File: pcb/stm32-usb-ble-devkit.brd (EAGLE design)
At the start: 90 x 50 mm, 98 parts, among them CN1 USB-MICROB-2TABS, CN2 USB-C-2.0-FEMALE, CN3 USB-C-2.0-FEMALE, Q2 AO3402, Q4 AO3401, Q6 AO3401, Q8 AO3401, U1 STM32F103-48LQFP, U2 STM32F205-64, U3 TUSB320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

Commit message: pcb: Replaced PSU BAS16 with better diode
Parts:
- D1: value BAS16 -> MBR0540T1; device tuetuopay:SOT23-3 -> tuetuopay:SOD123
- moved Q4 1.50 mm to (12.4, 47.4)
- moved D1 0.91 mm to (17.7, 47.2), turned to 0 degrees
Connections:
- net +5V: now also D1.C; no longer D1.3
- net STLINK_USB_VBUS: now also D1.A; no longer D1.1
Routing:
- net STLINK_USB_VBUS: track 41.4 -> 43.9 mm
- net +5V: track 65.0 -> 64.0 mm
- net USB_FS_HS_VBUS: track 6.31 -> 7.11 mm
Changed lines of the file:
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@@
 <attribute name="NAME" x="0.46" y="41.42" size="0.9" layer="25"/>
-</element>
-<element name="D1" library="tuetuopay" package="SOT23-3" value="BAS16" x="18.6" y="47.4" smashed="yes" rot="R270">
-<attribute name="NAME" x="20.03" y="49.21" size="0.9" layer="21" align="top-left"/>
 </element>
 <element name="JP10" library="pinhead" library_urn="urn:adsk.eagle:library:325" package="1X04" package3d_urn="urn:adsk.eagle:package:22407/2" value="" x="72.15" y="3.45" smashed="yes">
@@
 <attribute name="VALUE" x="39.637" y="14.07" size="1.27" layer="27" ratio="10" rot="R90"/>
 </element>
-<element name="Q4" library="tuetuopay" package="SOT23-3" value="AO3401" x="13.95" y="47.4" smashed="yes" rot="R270">
-<attribute name="NAME" x="15.23" y="46.36" size="0.9" layer="21" align="top-left"/>
+<element name="Q4" library="tuetuopay" package="SOT23-3" value="AO3401" x="12.45" y="47.4" smashed="yes" rot="R270">
+<attribute name="NAME" x="13.73" y="46.36" size="0.9" layer="21" align="top-left"/>
 </element>
 <element name="Q6" library="tuetuopay" package="SOT23-3" value="AO3401" x="15.45" y="12.3" smashed="yes" rot="R90">
@@
 <attribute name="NAME" x="61.615" y="22.765" size="0.9" layer="25" rot="R90"/>
 <attribute name="VALUE" x="59.295" y="21.635" size="1.27" layer="27" rot="R270"/>
+</element>
+<element name="D1" library="tuetuopay" package="SOD123" value="MBR0540T1" x="17.7" y="47.25" smashed="yes">
+<attribute name="NAME" x="16.75" y="48.4" size="0.9" layer="25"/>
+<attribute name="VALUE" x="16.6" y="44.95" size="1.27" layer="27"/>
 </element>
 </elements>
@@
 <via x="10.2" y="48.6" extent="1-16" drill="0.3"/>
 <via x="16.2" y="49.2" extent="1-16" drill="0.3"/>
-<via x="18" y="45" extent="1-16" drill="0.3"/>
+<via x="17.85" y="41.7" extent="1-16" drill="0.3"/>
 <via x="25.65" y="44.55" extent="1-16" drill="0.3"/>
 <via x="28.2" y="39.6" extent="1-16" drill="0.3"/>
@@
 <via x="71.4" y="7.8" extent="1-16" drill="0.3"/>
 <via x="54.6" y="9.6" extent="1-16" drill="0.3"/>
-<via x="12.6" y="40.35" extent="1-16" drill="0.3"/>
+<via x="12.75" y="42" extent="1-16" drill="0.3"/>
 <via x="13.5" y="39.6" extent="1-16" drill="0.3"/>
 <via x="4.35" y="27.3" extent="1-16" drill="0.3"/>
@@
 <via x="41.1" y="2.7" extent="1-16" drill="0.3"/>
 <via x="28.2" y="14.55" extent="1-16" drill="0.3"/>
-<via x="21.15" y="48" extent="1-16" drill="0.3"/>
+<via x="21.15" y="46.05" extent="1-16" drill="0.3"/>
 <via x="32.4" y="46.05" extent="1-16" drill="0.3"/>
 <via x="40.05" y="45.9" extent="1-16" drill="0.3"/>
@@
 <contactref element="U1" pad="47"/>
 <contactref element="R1" pad="2"/>
+<via x="16.2" y="45.9" extent="1-16" drill="0.3"/>
 </signal>
 <signal name="STLINK_PC13">
@@
 <contactref element="R16" pad="2"/>
 <contactref element="Q4" pad="1"/>
-<contactref element="D1" pad="1"/>
 <wire x1="44.03" y1="45.885" x2="44.03" y2="46.72" width="0.4" layer="1"/>
 <wire x1="44.03" y1="46.72" x2="43.65" y2="47.1" width="0.4" layer="1"/>
 <wire x1="44.03" y1="46.72" x2="50.67" y2="46.72" width="0.15" layer="1"/>
 <wire x1="50.67" y1="46.72" x2="51.7875" y2="47.85" width="0.15" layer="1"/>
-<wire x1="34.693" y1="47.1" x2="32.795" y2="48.998" width="0.4" layer="1"/>
-<wire x1="18.448" y1="48.998" x2="17.875" y2="48.425" width="0.4" layer="1"/>
+<wire x1="32.795" y1="48.998" x2="34.693" y2="47.1" width="0.4" layer="1"/>
 <wire x1="43.65" y1="47.1" x2="34.693" y2="47.1" width="0.4" layer="1"/>
-<wire x1="32.795" y1="48.998" x2="18.448" y2="48.998" width="0.4" layer="1"/>
-<wire x1="12.85" y1="48.35" x2="14.1" y2="48.35" width="0.4" layer="1"/>
-<wire x1="14.1" y1="48.35" x2="17.5" y2="48.35" width="0.4" layer="1"/>
-<wire x1="17.5" y1="48.35" x2="17.875" y2="48.425" width="0.4" layer="1"/>
+<contactref element="D1" pad="A"/>
+<wire x1="11.35" y1="48.35" x2="18.5" y2="48.35" width="0.4" layer="1"/>
+<wire x1="18.5" y1="48.35" x2="19.6" y2="47.25" width="0.4" layer="1"/>
+<wire x1="19.6" y1="47.25" x2="21.348" y2="48.998" width="0.4" layer="1"/>
+<wire x1="21.348" y1="48.998" x2="32.795" y2="48.998" width="0.4" layer="1"/>
 </signal>
 <signal name="STM_OSC_IN">
@@
 <contactref element="Q6" pad="2"/>
 <contactref element="Q8" pad="2"/>
-<contactref element="D1" pad="3"/>
 <contactref element="Q4" pad="3"/>
-<wire x1="15.05" y1="47.4" x2="19.7" y2="47.4" width="0.4" layer="1"/>
-<wire x1="15.05" y1="47.4" x2="12.105025" y2="47.4" width="0.4" layer="1"/>
-<wire x1="12.105025" y1="47.4" x2="11.8" y2="47.094975" width="0.4" layer="1"/>
-<wire x1="11.8" y1="45.805025" x2="12.139025" y2="45.466" width="0.4" layer="1"/>
-<wire x1="12.139025" y1="45.466" x2="14.7396625" y2="45.466" width="0.4" layer="1"/>
-<wire x1="14.7396625" y1="45.466" x2="15.45" y2="44.7556625" width="0.4" layer="1"/>
-<wire x1="11.8" y1="47.094975" x2="11.8" y2="45.805025" width="0.4" layer="1"/>
+<wire x1="13.55" y1="47.4" x2="10.605025" y2="47.4" width="0.4" layer="1"/>
+<wire x1="10.605025" y1="47.4" x2="10.3" y2="47.094975" width="0.4" layer="1"/>
+<wire x1="10.3" y1="45.805025" x2="10.639025" y2="45.466" width="0.4" layer="1"/>
+<wire x1="10.639025" y1="45.466" x2="14.5896625" y2="45.466" width="0.4" layer="1"/>
+<wire x1="14.5896625" y1="45.466" x2="15.45" y2="44.6056625" width="0.4" layer="1"/>
+<wire x1="10.3" y1="47.094975" x2="10.3" y2="45.805025" width="0.4" layer="1"/>
 <wire x1="14.9" y1="41.15" x2="14.9" y2="39.35" width="0.4" layer="1"/>
-<wire x1="15.45" y1="44.7556625" x2="15.45" y2="41.7" width="0.4" layer="1"/>
+<wire x1="15.45" y1="44.6056625" x2="15.45" y2="41.7" width="0.4" layer="1"/>
 <wire x1="15.45" y1="41.7" x2="14.9" y2="41.15" width="0.4" layer="1"/>
 <via x="14.9" y="39.35" extent="1-16" drill="0.3"/>
@@
 <wire x1="19.9" y1="35.75" x2="21.75" y2="35.75" width="0.4" layer="1"/>
 <wire x1="17.55" y1="38.1" x2="19.9" y2="35.75" width="0.4" layer="1"/>
+<contactref element="D1" pad="C"/>
+<wire x1="13.55" y1="47.4" x2="15.65" y2="47.4" width="0.4" layer="1"/>
+<wire x1="15.65" y1="47.4" x2="15.8" y2="47.25" width="0.4" layer="1"/>
 </signal>
 <signal name="STM_DBG_PIN2">
@@
 <contactref element="Q4" pad="2"/>
 <contactref element="JP7" pad="2"/>
-<wire x1="12.85" y1="46.45" x2="15.65" y2="46.45" width="0.4" layer="1"/>
-<wire x1="16.65" y1="45.45" x2="16.65" y2="43.35" width="0.4" layer="1"/>
-<wire x1="15.65" y1="46.45" x2="16.65" y2="45.45" width="0.4" layer="1"/>
+<wire x1="11.35" y1="46.45" x2="14.45" y2="46.45" width="0.4" layer="1"/>
+<wire x1="16.65" y1="44.25" x2="16.65" y2="43.35" width="0.4" layer="1"/>
+<wire x1="14.45" y1="46.45" x2="16.65" y2="44.25" width="0.4" layer="1"/>
 </signal>
 <signal name="SPI_CS">

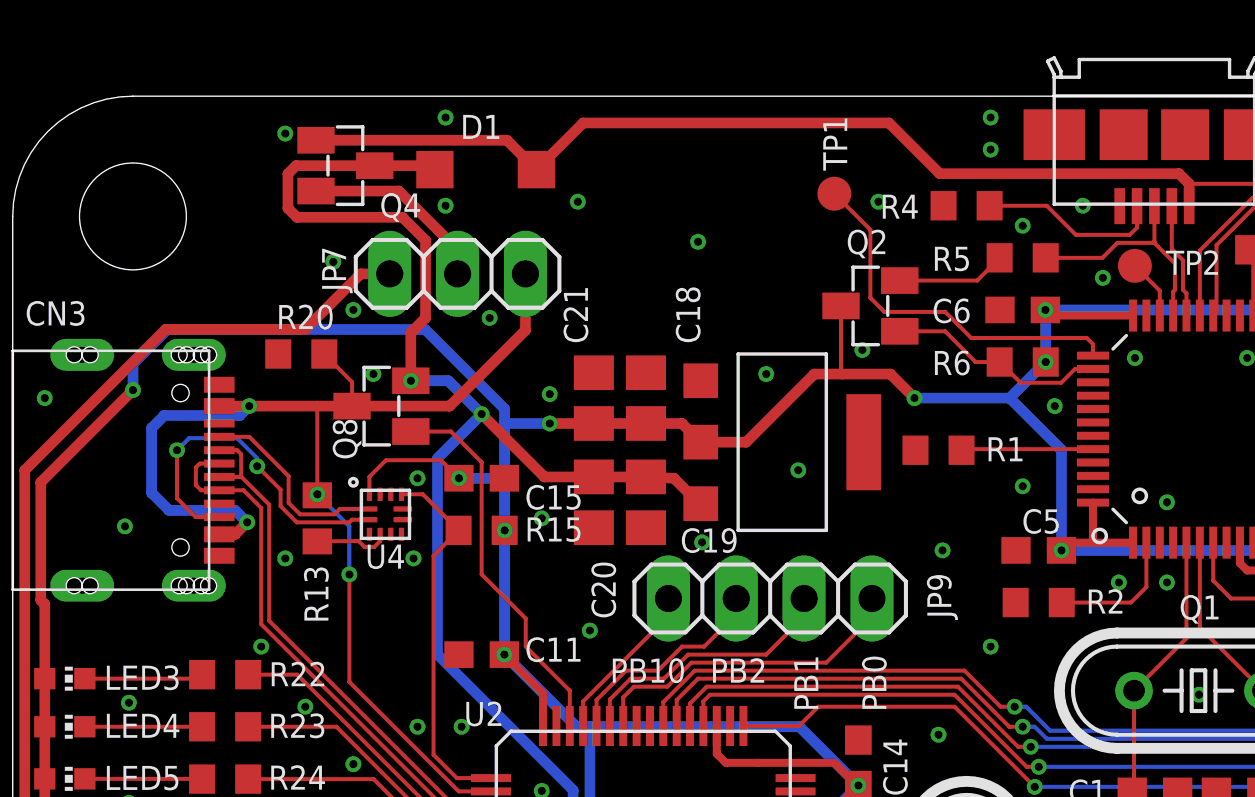
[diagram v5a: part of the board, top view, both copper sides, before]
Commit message: pcb: Replace PSU 0805 caps with 0603
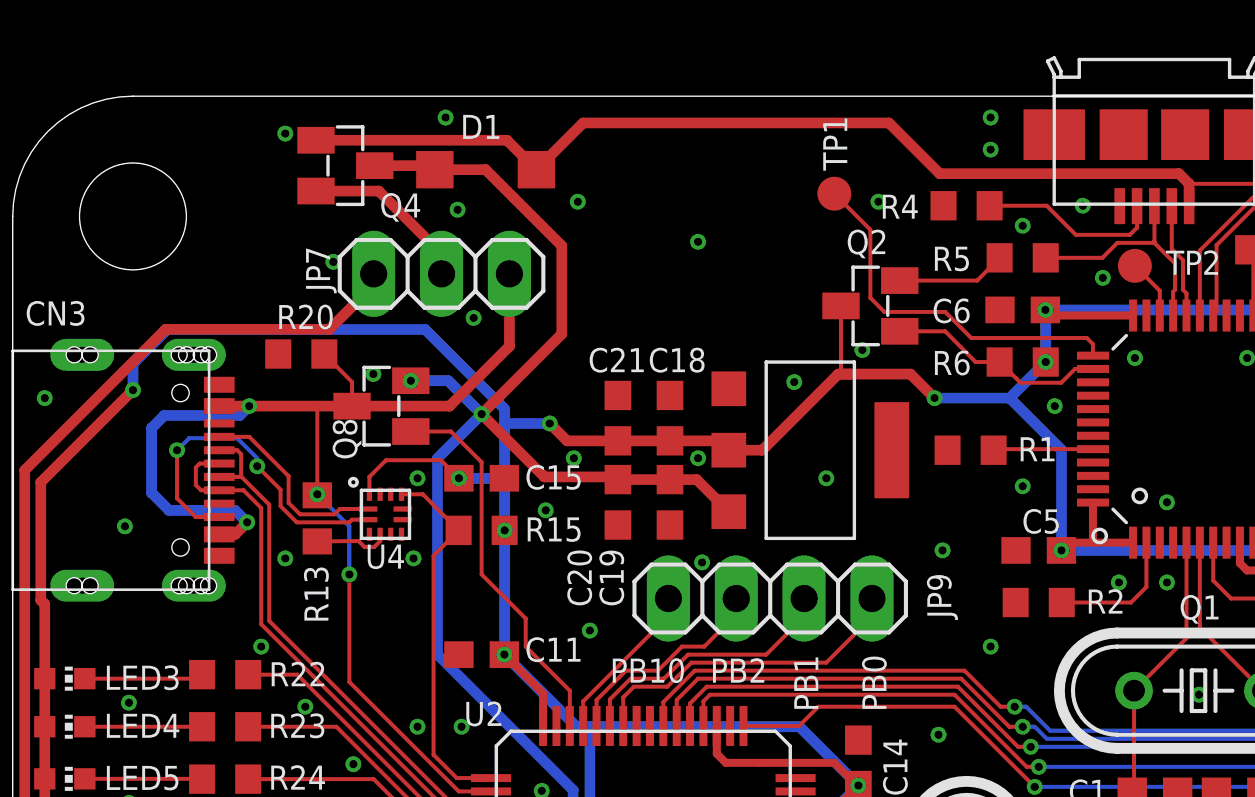
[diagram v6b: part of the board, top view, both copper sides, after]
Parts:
- C18, C19, C20, C21: device tuetuopay:0805 -> tuetuopay:0603
- moved R1 1.20 mm to (35.9, 36.8)
- moved C18 1.17 mm to (24.6, 38.0)
- moved C21 1.17 mm to (22.6, 38.0)
- moved U6 1.09 mm to (29.9, 36.8)
- moved C19 0.90 mm to (24.6, 34.8)
- moved C20 0.90 mm to (22.6, 34.8)
- moved JP7 0.60 mm to (16.1, 43.4)
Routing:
- net STLINK_BOOT0: track 4.94 -> 3.74 mm
- net +5V: track 64.0 -> 62.9 mm
- net USB_FS_HS_VBUS: track 7.11 -> 6.42 mm
- net +3V3: track 274.8 -> 275.3 mm

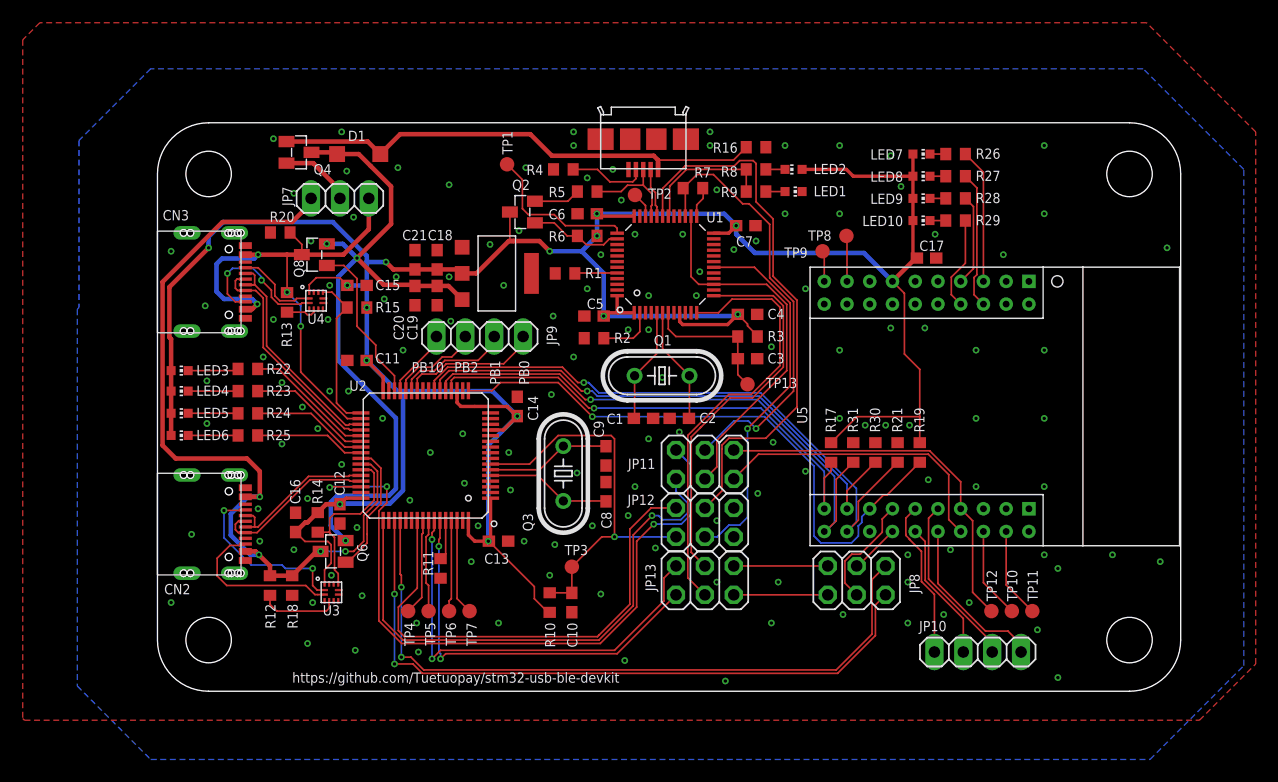
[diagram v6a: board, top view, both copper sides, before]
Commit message: pcb: Switch OTG PSU MOSFET to dedicated IC
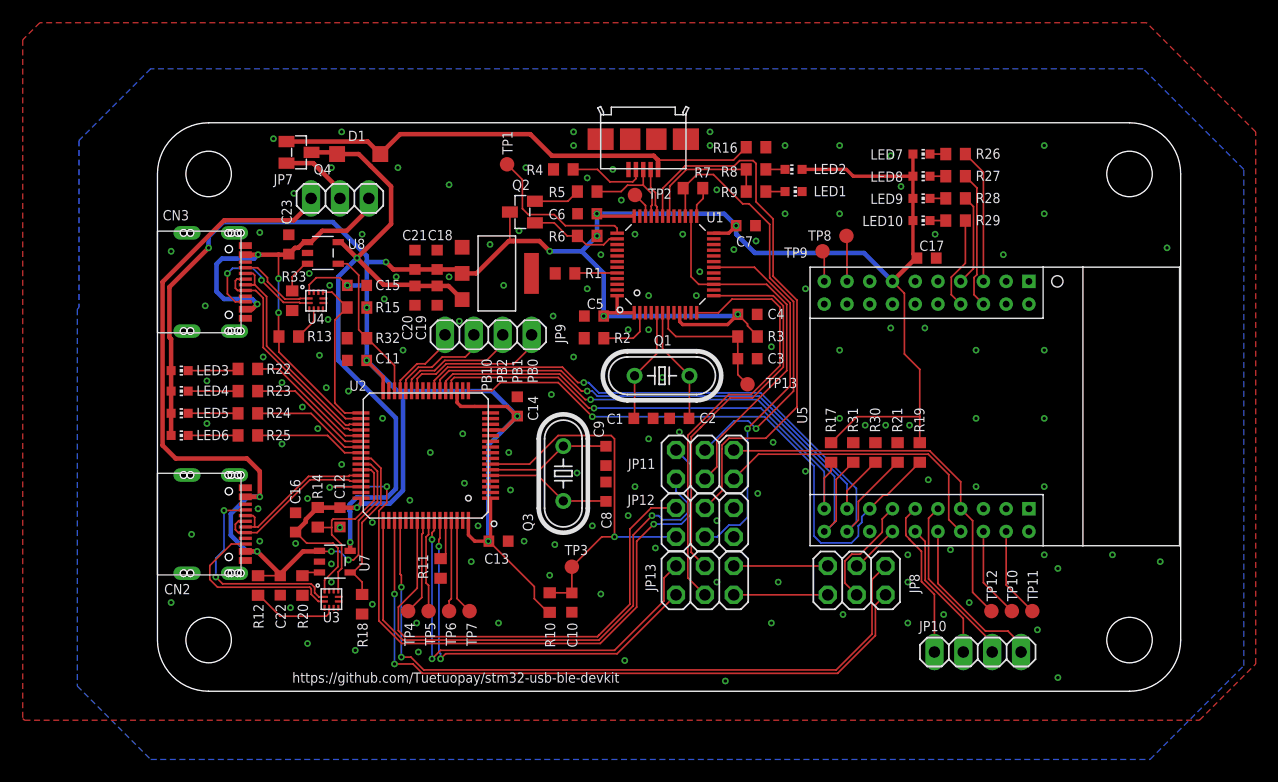
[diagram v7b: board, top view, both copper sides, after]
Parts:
- removed Q6, Q8: AO3401, tuetuopay:SOT23-3
- added C22, C23: 10u, tuetuopay:0603
- added R32: 10k, tuetuopay:R0603
- added R33: 68k, tuetuopay:R0603
- added U7, U8: SY6280, tuetuopay:SOT23-5
- R18: value 100k -> 10k
- R20: value 100k -> 68k
- moved R20 31.1 mm to (12.8, 9.30), turned to 90 degrees
- moved R18 6.37 mm to (18.0, 7.65)
- moved R13 3.00 mm to (11.6, 31.2), turned to 0 degrees
- moved R12 1.05 mm to (8.85, 9.30)
- moved JP9 0.76 mm to (29.1, 31.4)
- moved U3 0.60 mm to (15.3, 8.10)
- moved R14 0.45 mm to (14.1, 15.3)
- moved C12 0.30 mm to (16.1, 15.3)
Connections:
- new net USB_FS_ISET: R20.2, U7.3
- new net USB_HS_ISET: R33.2, U8.3
- net +5V: now also U7.5, U8.5; no longer Q6.2, Q8.2
- net GND: now also C22.2, C23.2, R32.1, R33.1, U7.2, U8.2
- net USB_FS_ON: now also R18.2, U7.4; no longer Q6.1
- net USB_FS_VBUS: now also C22.1, U7.1; no longer Q6.3, R18.2
- net USB_HS_ON: now also R32.2, U8.4; no longer Q8.1
- net USB_HS_VBUS: now also C23.1, U8.1; no longer Q8.3, R20.2
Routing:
- net USB_FS_ON: track 11.8 -> 15.0 mm
- net USB_HS_VBUS: track 46.4 -> 43.3 mm
- net USB_HS_ISET: track 0.00 -> 3.06 mm
- net USB_FS_CC1: track 15.9 -> 18.5 mm
- net USB_FS_VBUS: track 73.4 -> 75.8 mm
- net +5V: track 62.9 -> 60.6 mm, vias 3 -> 2
- net USB_FS_CC2: track 14.6 -> 16.3 mm
- net USB_FS_ISET: track 0.00 -> 1.62 mm
- net STM_DBG_PIN2: track 8.13 -> 9.29 mm
- net STM_DBG_PIN0: track 12.3 -> 13.3 mm
- net STM_DBG_PIN3: track 6.09 -> 6.99 mm
- net STM_DBG_PIN1: track 10.2 -> 11.1 mm
- net USB_FS_ID: track 15.4 -> 16.1 mm
- net USB_FS_VBUS_DET: track 6.99 -> 7.61 mm
- net USB_HS_CC1: track 7.44 -> 6.93 mm
